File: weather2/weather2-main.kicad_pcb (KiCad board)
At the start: 2 copper layers, 30 x 85 mm, 1 part, among them U1 ESP32-WROOM-32

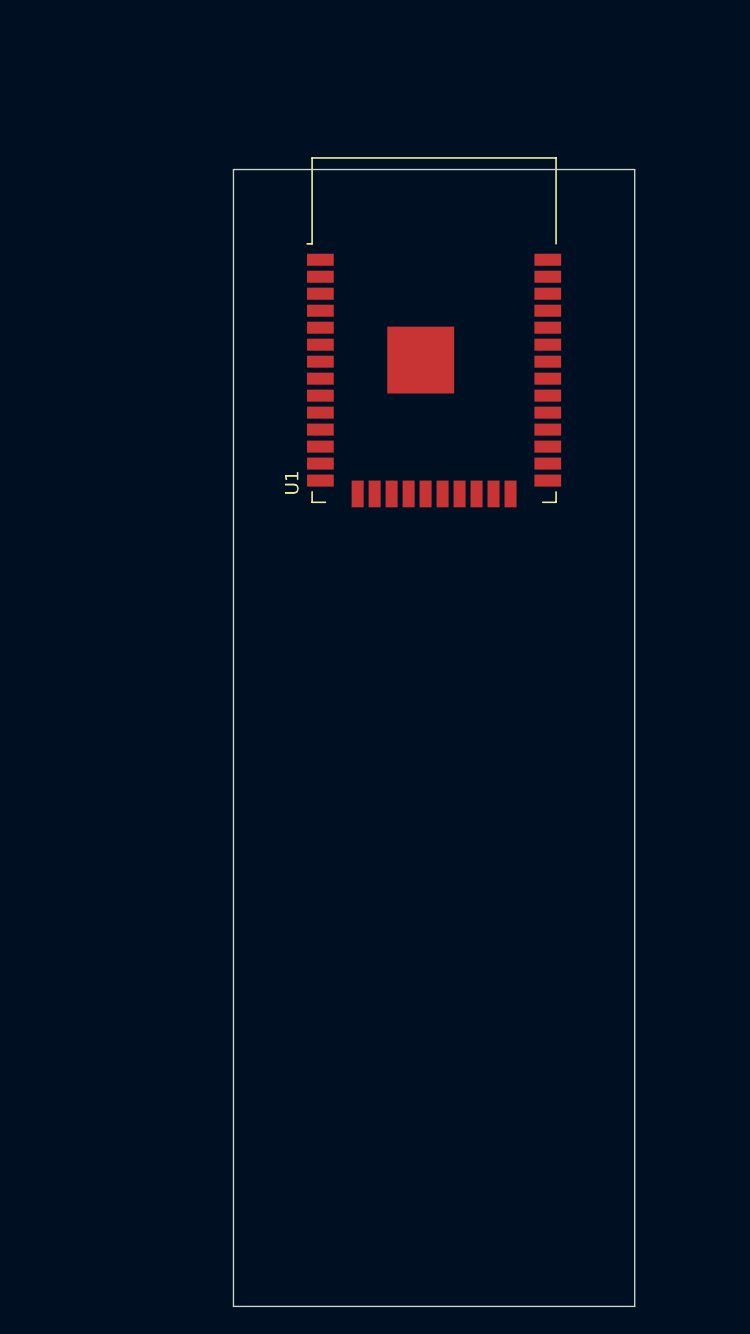
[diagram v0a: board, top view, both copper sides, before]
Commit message: Complete schematic. Start of layout.
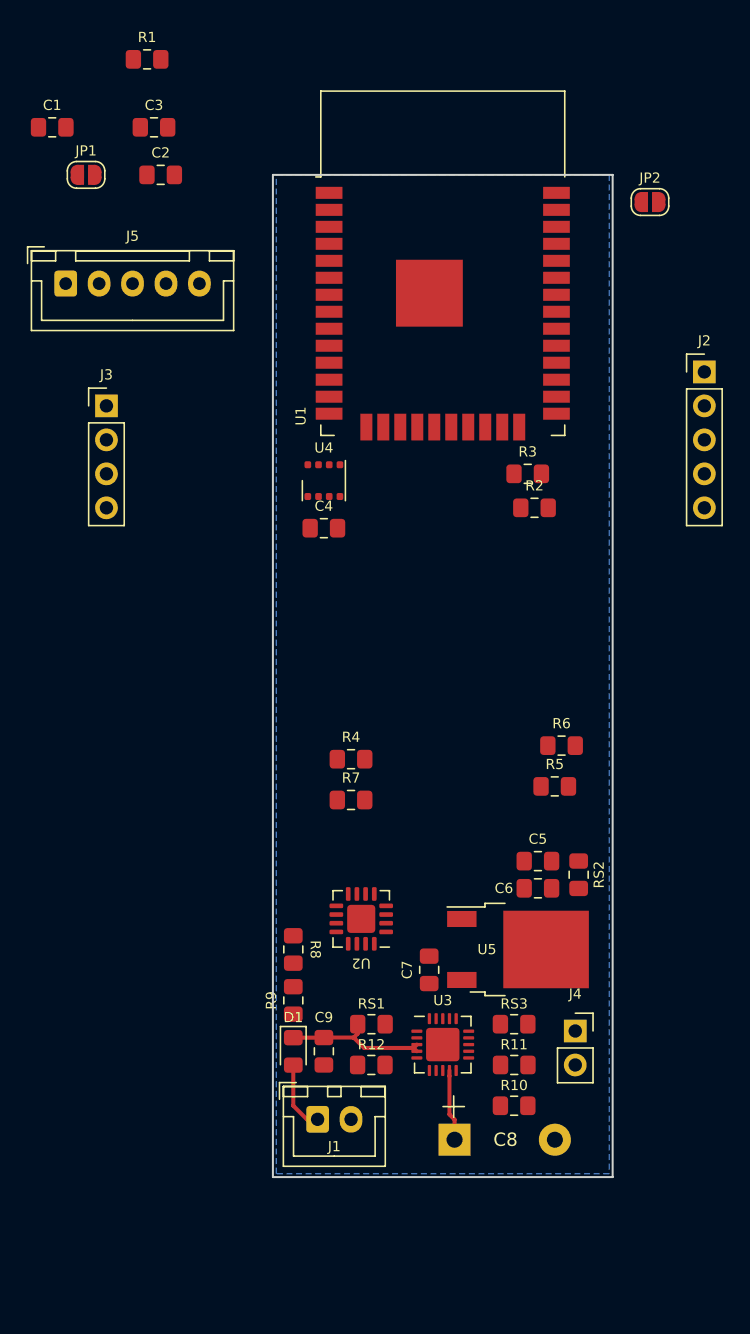
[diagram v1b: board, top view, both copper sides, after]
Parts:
- added C1: 1nf, Capacitor_SMD:C_0805_2012Metric_Pad1.15x1.40mm_HandSolder, F.Cu at (91.4, 21.8)
- added C2: 1uf, Capacitor_SMD:C_0805_2012Metric_Pad1.15x1.40mm_HandSolder, F.Cu at (99.6, 25.4)
- added C3: 100uf, Capacitor_SMD:C_0805_2012Metric_Pad1.15x1.40mm_HandSolder, F.Cu at (99.1, 21.8)
- added C4: 100nf, Capacitor_SMD:C_0805_2012Metric_Pad1.15x1.40mm_HandSolder, F.Cu at (111.8, 51.8)
- added C5: 1uf, Capacitor_SMD:C_0805_2012Metric_Pad1.15x1.40mm_HandSolder, F.Cu at (127.8, 76.7)
- added C6: 100uf, Capacitor_SMD:C_0805_2012Metric_Pad1.15x1.40mm_HandSolder, F.Cu at (127.8, 78.7)
- added C7: 100uf, Capacitor_SMD:C_0805_2012Metric_Pad1.15x1.40mm_HandSolder, F.Cu at (119.6, 84.8)
- added C8: 4700uf/10v, Weather2:CP_Radial_D16.0mm_P7.50mm-SpaceSaver, F.Cu at (125.3, 97.5)
- added C9: 10uf, Capacitor_SMD:C_0805_2012Metric_Pad1.15x1.40mm_HandSolder, F.Cu at (111.8, 90.9)
- added D1: D, Diode_SMD:D_0805_2012Metric_Pad1.15x1.40mm_HandSolder, F.Cu at (109.5, 90.9)
- added J1: Solar In, Connector_JST:JST_XH_B2B-XH-A_1x02_P2.50mm_Vertical, F.Cu at (111.3, 96.0)
- added J2: UART, Connector_PinHeader_2.54mm:PinHeader_1x05_P2.54mm_Vertical, F.Cu at (140.2, 40.1)
- added J3: JTAG, Connector_PinHeader_2.54mm:PinHeader_1x04_P2.54mm_Vertical, F.Cu at (95.5, 42.7)
- added J4: BATT, Connector_PinSocket_2.54mm:PinSocket_1x02_P2.54mm_Vertical, F.Cu at (130.6, 89.4)
- added J5: EXT SENSE, Connector_JST:JST_XH_B5B-XH-A_1x05_P2.50mm_Vertical, F.Cu at (92.5, 33.5)
- added JP1: SolderJumper_2_Open, Jumper:SolderJumper-2_P1.3mm_Open_RoundedPad1.0x1.5mm, F.Cu at (94.0, 25.4)
- added JP2: SolderJumper_2_Open, Jumper:SolderJumper-2_P1.3mm_Open_RoundedPad1.0x1.5mm, F.Cu at (136.1, 27.4)
- added R1: 10k, Resistor_SMD:R_0805_2012Metric_Pad1.15x1.40mm_HandSolder, F.Cu at (98.5, 16.8)
- added R10: 2k, Resistor_SMD:R_0805_2012Metric_Pad1.15x1.40mm_HandSolder, F.Cu at (126.0, 95.0)
- added R11: 100k, Resistor_SMD:R_0805_2012Metric_Pad1.15x1.40mm_HandSolder, F.Cu at (126.0, 91.9)
- added R12: 10k, Resistor_SMD:R_0805_2012Metric_Pad1.15x1.40mm_HandSolder, F.Cu at (115.3, 91.9)
- added R2: 10k, Resistor_SMD:R_0805_2012Metric_Pad1.15x1.40mm_HandSolder, F.Cu at (127.5, 50.3)
- added R3: 10k, Resistor_SMD:R_0805_2012Metric_Pad1.15x1.40mm_HandSolder, F.Cu at (127.0, 47.8)
- added R4: 10k, Resistor_SMD:R_0805_2012Metric_Pad1.15x1.40mm_HandSolder, F.Cu at (113.8, 69.1)
- added R5: 10k, Resistor_SMD:R_0805_2012Metric_Pad1.15x1.40mm_HandSolder, F.Cu at (129.0, 71.1)
- added R6: 10k, Resistor_SMD:R_0805_2012Metric_Pad1.15x1.40mm_HandSolder, F.Cu at (129.5, 68.1)
- added R7: 10k, Resistor_SMD:R_0805_2012Metric_Pad1.15x1.40mm_HandSolder, F.Cu at (113.8, 72.1)
- added R8: 270k, Resistor_SMD:R_0805_2012Metric_Pad1.15x1.40mm_HandSolder, F.Cu at (109.5, 83.3)
- added R9: 100k, Resistor_SMD:R_0805_2012Metric_Pad1.15x1.40mm_HandSolder, F.Cu at (109.5, 87.1)
- added RS1: 0.1, Resistor_SMD:R_0805_2012Metric_Pad1.15x1.40mm_HandSolder, F.Cu at (115.3, 88.9)
- added RS2: 0.1, Resistor_SMD:R_0805_2012Metric_Pad1.15x1.40mm_HandSolder, F.Cu at (130.8, 77.7)
- added RS3: 0.1, Resistor_SMD:R_0805_2012Metric_Pad1.15x1.40mm_HandSolder, F.Cu at (126.0, 88.9)
- added U2: INA3221, Package_DFN_QFN:Texas_RGV_S-PVQFN-N16_EP2.1x2.1mm, F.Cu at (114.6, 81.0)
- added U3: MCP73871-2CC, Package_DFN_QFN:QFN-20-1EP_4x4mm_P0.5mm_EP2.5x2.5mm, F.Cu at (120.7, 90.4)
- added U4: BME680, Package_LGA:Bosch_LGA-8_3x3mm_P0.8mm_ClockwisePinNumbering, F.Cu at (111.8, 48.3)
- added U5: LM1117-3.3, Package_TO_SOT_SMD:TO-252-2, F.Cu at (126.3, 83.3)
- moved U1 5.04 mm to (120.7, 35.0)
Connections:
- net Net-(U1-Pad1) renamed GND
- U1 pad 10: Net-(U1-Pad10) -> /EX_WIND_DIR
- U1 pad 11: Net-(U1-Pad11) -> /STAT2
- U1 pad 12: Net-(U1-Pad12) -> /PG
- U1 pad 13: Net-(U1-Pad13) -> /TMS
- U1 pad 14: Net-(U1-Pad14) -> /TDI
- U1 pad 16: Net-(U1-Pad16) -> /TCK
- U1 pad 2: Net-(U1-Pad2) -> +3V3
- U1 pad 23: Net-(U1-Pad23) -> /SDA
- U1 pad 24: Net-(U1-Pad24) -> /SCL
- U1 pad 26: Net-(U1-Pad26) -> /STAT1
- U1 pad 5: Net-(U1-Pad5) -> /EX_RAIN
- U1 pad 6: Net-(U1-Pad6) -> /CRIT
- U1 pad 7: Net-(U1-Pad7) -> /WARN
- U1 pad 8: Net-(U1-Pad8) -> /EX_WIND_SPD
- U1 pad 9: Net-(U1-Pad9) -> /TC
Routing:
- net +6V: track 0.00 -> 16.5 mm
- net Net-(D1-Pad2): track 0.00 -> 5.28 mm
- added copper zone on B.Cu, net GND
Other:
- board size 30 x 85 mm -> 25.4 x 74.9 mm
- net class Default: clearance 0.2 -> 0.1524; trace_width 0.25 -> 0.1524; via_dia 0.8 -> 0.6858; via_drill 0.4 -> 0.3302
- rule pad_to_mask_clearance: 0.051 -> 0.0508
- rule trace_clearance: 0.2 -> 0.1524
- rule trace_min: 0.2 -> 0.1524
- rule via_min_drill: 0.3 -> 0.254
- rule via_min_size: 0.4 -> 0.508

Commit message: 1.0 board!
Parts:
- removed J3: JTAG, Connector_PinHeader_2.54mm:PinHeader_1x04_P2.54mm_Vertical
- removed JP1, JP2: SolderJumper_2_Open, Jumper:SolderJumper-2_P1.3mm_Open_RoundedPad1.0x1.5mm
- added D2: D, Diode_SMD:D_0805_2012Metric_Pad1.15x1.40mm_HandSolder, F.Cu at (126.7, 68.2)
- C1: value 1nf -> 100nf
- J1: footprint Connector_JST:JST_XH_B2B-XH-A_1x02_P2.50mm_Vertical -> Connector_PinHeader_2.54mm:PinHeader_1x02_P2.54mm_Vertical
- J2: footprint Connector_PinHeader_2.54mm:PinHeader_1x05_P2.54mm_Vertical -> Connector_PinHeader_2.54mm:PinHeader_1x06_P2.54mm_Vertical
- J4: footprint Connector_PinSocket_2.54mm:PinSocket_1x02_P2.54mm_Vertical -> Connector_PinHeader_2.54mm:PinHeader_1x02_P2.54mm_Vertical
- J5: footprint Connector_JST:JST_XH_B5B-XH-A_1x05_P2.50mm_Vertical -> Connector_PinHeader_2.54mm:PinHeader_1x05_P2.54mm_Vertical
- moved R1 62.5 mm to (125.9, 73.0), turned to 180 degrees
- moved C1 60.1 mm to (125.9, 71.1)
- moved J5 49.9 mm to (110.5, 80.0), turned to 180 degrees
- moved C3 32.4 mm to (109.7, 52.5), turned to 270 degrees
- moved J2 29.5 mm to (130.7, 68.1)
- moved U4 29.3 mm to (121.0, 76.1), turned to 90 degrees
- moved C2 25.4 mm to (109.7, 48.6), turned to 90 degrees
- moved C4 23.4 mm to (121.0, 73.3)
- moved R3 20.9 mm to (122.8, 68.2), turned to 270 degrees
- moved U1 20.6 mm to (120.9, 55.6)
- moved R6 19.6 mm to (114.2, 80.3), turned to 90 degrees
- moved C8 18.2 mm to (110.5, 87.0), turned to 90 degrees
- moved R2 18.1 mm to (124.7, 68.2), turned to 270 degrees
- moved C7 17.9 mm to (131.2, 98.6), turned to 0 degrees
- moved R8 17.6 mm to (121.5, 96.1), turned to 180 degrees
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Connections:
- C1 pad 2: Net-(C1-Pad2) -> /EN
- J2 pad 1: Net-(J2-Pad1) -> Net-(D2-Pad1)
- J2 pad 3: +3V3 -> Net-(J2-Pad3)
- J2 pad 4: Net-(J2-Pad4) -> +3V3
- J2 pad 5: GND -> /EN
- R1 pad 1: Net-(C1-Pad2) -> /EN
- U1 pad 12: /PG -> /STAT1
- U1 pad 13: /TMS -> Net-(U1-Pad13)
- U1 pad 14: /TDI -> Net-(U1-Pad14)
- U1 pad 16: /TCK -> Net-(U1-Pad16)
- U1 pad 25: Net-(JP2-Pad2) -> Net-(D2-Pad1)
- U1 pad 26: /STAT1 -> /PG
- U1 pad 3: Net-(C1-Pad2) -> /EN
- U1 pad 34: Net-(J2-Pad1) -> Net-(J2-Pad2)
- U1 pad 35: Net-(J2-Pad2) -> Net-(J2-Pad3)
- U1 pad 6: /CRIT -> /WARN
- U1 pad 7: /WARN -> /CRIT
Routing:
- net +3V3: track 0.00 -> 143.4 mm, vias 0 -> 7
- net /EN: track 0.00 -> 61.0 mm, vias 0 -> 2
- net GND: track 0.00 -> 53.8 mm, vias 0 -> 13
- net /STAT2: track 0.00 -> 49.2 mm, vias 0 -> 4
- net /STAT1: track 0.00 -> 48.0 mm, vias 0 -> 4
- net /PG: track 0.00 -> 35.2 mm, vias 0 -> 2
- net /TC: track 0.00 -> 33.4 mm, vias 0 -> 2
- net +6V: track 16.5 -> 49.5 mm, vias 0 -> 6
- net /CRIT: track 0.00 -> 29.9 mm
- net /WARN: track 0.00 -> 29.7 mm
- net Net-(J2-Pad3): track 0.00 -> 24.3 mm
- net Net-(C7-Pad1): track 0.00 -> 22.9 mm
- net /SCL: track 0.00 -> 21.4 mm
- net /SDA: track 0.00 -> 20.6 mm
- net Net-(J2-Pad2): track 0.00 -> 20.3 mm
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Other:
- board size 25.4 x 74.9 mm -> 25.4 x 54.5 mm
- board text added: "+"
- board text added: "05.03.2020"
- board text added: "Batt"
- board text added: "Rain"
- board text added: "Solar"
- board text added: "ToonyWeather 1.0"
- board text added: "Wind Dir"
- board text added: "Wind Spd"

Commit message: Update to KiCad 7.
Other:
- net class Default removed
